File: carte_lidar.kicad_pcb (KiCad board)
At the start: 2 copper layers, 68 x 68 mm, 26 parts, among them J1 Conn_01x03_Pin, J2 Conn_01x02_Pin, J3 Conn_01x05_Socket, J4 Conn_01x02, J5 Conn_01x08_Pin, U1 TPS54302, U2 RP2040, U3 CH340C

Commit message: v1
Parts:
- removed U3: CH340C, Package_SO:SOIC-16_3.9x9.9mm_P1.27mm
- added R5: 330R, Resistor_SMD:R_0603_1608Metric, F.Cu at (84.5, 102.5)
- J5: value Conn_01x08_Pin -> Conn_01x04_Socket; footprint Connector_PinHeader_1.00mm:PinHeader_1x08_P1.00mm_Vertical -> Connector_PinSocket_2.54mm:PinSocket_1x04_P2.54mm_Vertical
- U2: value RP2040 -> Pico; footprint Package_DFN_QFN:QFN-56-1EP_7x7mm_P0.4mm_EP3.2x3.2mm -> MCU_RaspberryPi_and_Boards:RPi_Pico_SMD_TH
- moved J3 50.8 mm to (86.3, 76.0), turned to -90 degrees
- moved C6 43.0 mm to (91.5, 126.5), turned to -90 degrees
- moved J4 42.1 mm to (125.9, 104.0), turned to 90 degrees
- moved C8 42.1 mm to (93.7, 126.4), turned to -90 degrees
- moved C7 41.2 mm to (89.3, 126.5), turned to -90 degrees
- moved J5 40.4 mm to (84.8, 91.9)
- moved J1 40.1 mm to (75.8, 94.3), turned to -90 degrees
- moved C9 34.2 mm to (91.7, 119.6)
- moved R4 33.7 mm to (125.3, 109.2)
- moved R3 33.0 mm to (125.3, 110.4)
- moved C10 32.7 mm to (89.5, 119.6)
- moved L1 30.9 mm to (84.0, 123.5), turned to 0 degrees
- moved C3 25.5 mm to (86.1, 118.9)
- moved J2 24.9 mm to (81.0, 107.0), turned to -90 degrees
- moved R1 21.4 mm to (76.3, 119.4), turned to 90 degrees
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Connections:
- J1 pad 1: unconnected-(J1-Pin_1-Pad1) -> 5V
- J1 pad 2: unconnected-(J1-Pin_2-Pad2) -> GND
- J1 pad 3: unconnected-(J1-Pin_3-Pad3) -> /led
- J3 pad 1: unconnected-(J3-Pin_1-Pad1) -> 5V
- J3 pad 2: unconnected-(J3-Pin_2-Pad2) -> /lidar_tx
- J3 pad 3: unconnected-(J3-Pin_3-Pad3) -> /lidar_rx
- J3 pad 4: unconnected-(J3-Pin_4-Pad4) -> GND
- J3 pad 5: unconnected-(J3-Pin_5-Pad5) -> /motoct
- J5 pad 1: unconnected-(J5-Pin_1-Pad1) -> 5V
- J5 pad 2: unconnected-(J5-Pin_2-Pad2) -> GND
- J5 pad 3: unconnected-(J5-Pin_3-Pad3) -> /scl
- J5 pad 4: unconnected-(J5-Pin_4-Pad4) -> /sda
- U2 pad 1: Net-(U2-IOVDD-Pad1) -> AU
- U2 pad 10: Net-(U2-IOVDD-Pad1) -> unconnected-(U2-GPIO7-Pad10)
- U2 pad 11: unconnected-(U2-GPIO8-Pad11) -> /sda
- U2 pad 12: unconnected-(U2-GPIO9-Pad12) -> /scl
- U2 pad 13: unconnected-(U2-GPIO10-Pad13) -> GND
- U2 pad 15: unconnected-(U2-GPIO12-Pad15) -> /motoct
- U2 pad 16: unconnected-(U2-GPIO13-Pad16) -> /lidar_rx
- U2 pad 17: unconnected-(U2-GPIO14-Pad17) -> /lidar_tx
- U2 pad 18: unconnected-(U2-GPIO15-Pad18) -> GND
- U2 pad 22: Net-(U2-IOVDD-Pad1) -> unconnected-(U2-GPIO17-Pad22)
- U2 pad 23: Net-(U2-DVDD-Pad23) -> GND
- U2 pad 28: unconnected-(U2-GPIO17-Pad28) -> GND
- U2 pad 3: unconnected-(U2-GPIO1-Pad3) -> GND
- U2 pad 33: Net-(U2-IOVDD-Pad1) -> unconnected-(U2-AGND-Pad33)
- U2 pad 38: unconnected-(U2-GPIO26_ADC0-Pad38) -> GND
- U2 pad 39: unconnected-(U2-GPIO27_ADC1-Pad39) -> 5V
- U2 pad 40: unconnected-(U2-GPIO28_ADC2-Pad40) -> 5V
- U2 pad 42: Net-(U2-IOVDD-Pad1) -> GND
- U2 pad 6: unconnected-(U2-GPIO4-Pad6) -> Net-(U2-GPIO4)
- U2 pad 8: unconnected-(U2-GPIO6-Pad8) -> GND
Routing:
- net 5V: track 0.00 -> 133.8 mm
- net GND: track 0.00 -> 40.0 mm, vias 0 -> 1
- net Net-(U2-GPIO4): track 0.00 -> 34.2 mm
- net /scl: track 0.00 -> 31.9 mm
- net /sda: track 0.00 -> 31.7 mm
- net /lidar_rx: track 0.00 -> 31.6 mm
- net /lidar_tx: track 0.00 -> 31.6 mm
- net /motoct: track 0.00 -> 30.6 mm
- net AU: track 0.00 -> 19.3 mm
- net /led: track 0.00 -> 10.3 mm
- net Net-(U1-FB): track 0.00 -> 9.81 mm
- net Net-(U1-SW): track 0.00 -> 9.74 mm
- net Net-(J4-Pin_1): track 0.00 -> 5.05 mm
- net Net-(U1-BOOT): track 0.00 -> 2.37 mm
- net 24V: track 0.00 -> 1.72 mm
- added copper zone on F.Cu, net 24V
- added copper zone on F.Cu, net 5V
- added copper zone on B.Cu, net GND
- added copper zone on F.Cu, net GND
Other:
- board text added: "Accelerometer"
- board text added: "LED"
- board text added: "LIDAR"
- board text added: "VIN - 24V"

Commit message: update all
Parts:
- added C21: 0.1uF 10V, Capacitor_SMD:C_0402_1005Metric, F.Cu at (101.8, 103.6)
- added C22: 220nF 50V, Capacitor_SMD:C_0402_1005Metric, F.Cu at (69.7, 107.7)
- added C23: 2.2nF 10V, Capacitor_SMD:C_0402_1005Metric, F.Cu at (103.4, 98.3)
- added C24: 0.1uF 10V, Capacitor_SMD:C_0402_1005Metric, F.Cu at (103.4, 101.8)
- added C25: 0.1uF 10V, Capacitor_SMD:C_0402_1005Metric, F.Cu at (108.9, 88.0)
- added C26: 1uF 10V, Capacitor_SMD:C_0402_1005Metric, F.Cu at (108.6, 90.8)
- added C27: 0.1uF 10V, Capacitor_SMD:C_0402_1005Metric, F.Cu at (96.8, 89.0)
- added C28: 220nF 16V, Capacitor_SMD:C_0402_1005Metric, F.Cu at (119.0, 79.4)
- added D1: MBR120VLSFT1G, Diode_SMD:D_SOD-123F, F.Cu at (123.2, 101.4)
- added J6: USB_C_Receptacle_USB2.0, Connector_USB:USB_C_Receptacle_GCT_USB4105-xx-A_16P_TopMnt_Horizontal, F.Cu at (125.7, 94.5)
- added LED1: YELLOW, LED_SMD:LED_0805_2012Metric, F.Cu at (124.8, 104.8)
- added LED2: YELLOW, LED_SMD:LED_0805_2012Metric, F.Cu at (87.9, 91.2)
- added R11: 5.1k, Resistor_SMD:R_0402_1005Metric, F.Cu at (119.0, 94.0)
- added R12: 5.1k, Resistor_SMD:R_0402_1005Metric, F.Cu at (119.0, 92.8)
- added R13: 27R, Resistor_SMD:R_0402_1005Metric, F.Cu at (115.7, 96.8)
- added R14: 27R, Resistor_SMD:R_0402_1005Metric, F.Cu at (115.7, 95.7)
- added R15: 1k, Resistor_SMD:R_0402_1005Metric, F.Cu at (88.9, 93.4)
- added R16: 10k, Capacitor_SMD:C_0402_1005Metric, F.Cu at (96.9, 91.0)
- added R17: 5.1k, Resistor_SMD:R_0402_1005Metric, F.Cu at (68.3, 105.9)
- added R18: 1k, Resistor_SMD:R_0402_1005Metric, F.Cu at (70.0, 106.4)
- added R6: 1k, Resistor_SMD:R_0402_1005Metric, F.Cu at (104.6, 73.3)
- added R7: 100k, Resistor_SMD:R_0402_1005Metric, F.Cu at (104.6, 74.7)
- added R8: 1k, Resistor_SMD:R_0402_1005Metric, F.Cu at (122.1, 103.8)
- added SW1: SW_Push, Button_Switch_SMD:SW_SPST_B3U-1000P, F.Cu at (104.1, 69.9)
- added U3: W25Q128JVS, Package_SO:SOIC-8_5.23x5.23mm_P1.27mm, F.Cu at (113.6, 80.8)
- added U5: USBLC6-2P6, Package_TO_SOT_SMD:SOT-666, F.Cu at (119.1, 96.2)
- added U6: NM/AMS1117-3.3, Package_TO_SOT_SMD:SOT-223-3_TabPin2, F.Cu at (116.1, 103.8)
- added U7: MPU-6000, Sensor_Motion:InvenSense_QFN-24_4x4mm_P0.5mm, F.Cu at (100.0, 100.0)
- added X1: S2D12.000000B20F30T, Oscillator:Oscillator_SMD_ECS_2520MV-xxx-xx-4Pin_2.5x2.0mm, F.Cu at (93.6, 90.0)
- J1, J2, J3, J4: moved to B.Cu
- J5: value Conn_01x04_Socket -> Conn_01x02_Pin; footprint Connector_PinSocket_2.54mm:PinSocket_1x04_P2.54mm_Vertical -> Connector_PinHeader_2.54mm:PinHeader_1x02_P2.54mm_Vertical
- U2: value Pico -> RP2040; footprint MCU_RaspberryPi_and_Boards:RPi_Pico_SMD_TH -> Package_DFN_QFN:QFN-56-1EP_7x7mm_P0.4mm_EP3.2x3.2mm_ThermalVias
- moved H2 59.0 mm to (74.5, 85.2)
- moved C6 35.7 mm to (77.6, 93.6), turned to 90 degrees
- moved C8 34.8 mm to (81.8, 93.7), turned to 90 degrees
- moved C7 34.2 mm to (79.7, 93.7), turned to 90 degrees
- moved H3 29.6 mm to (100.0, 129.5)
- moved C10 29.5 mm to (75.5, 93.6)
- moved H1 29.5 mm to (125.5, 85.2)
- moved J4 27.9 mm to (109.0, 126.3), turned to 180 degrees
- moved C9 27.1 mm to (83.9, 93.7)
- moved J5 25.2 mm to (99.0, 71.1), turned to 180 degrees
- moved L1 24.6 mm to (78.1, 99.7), turned to 90 degrees
- moved J3 22.7 mm to (89.5, 98.5)
- moved C5 21.8 mm to (84.8, 99.4), turned to -90 degrees
- moved R1 21.8 mm to (82.6, 98.5), turned to -90 degrees
- moved R5 21.3 mm to (88.4, 81.6)
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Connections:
- net 24V renamed /power/VBAT
- C10 pad 1: 5V -> +5V
- C5 pad 1: 5V -> +5V
- C6 pad 1: 5V -> +5V
- C7 pad 1: 5V -> +5V
- C8 pad 1: 5V -> +5V
- C9 pad 1: 5V -> +5V
- J1 pad 1: 5V -> +5V
- J1 pad 3: /led -> Net-(J1-Pin_3)
- J3 pad 1: 5V -> +5V
- J5 pad 1: 5V -> Net-(J5-Pin_1)
- L1 pad 2: 5V -> +5V
- R1 pad 1: 5V -> +5V
- R3 pad 1: AU -> /AU
- R4 pad 1: 5V -> +3V3
- R5 pad 1: /led -> Net-(J1-Pin_3)
- R5 pad 2: Net-(U2-GPIO4) -> /led
- U2 pad 1: AU -> +3V3
- U2 pad 10: unconnected-(U2-GPIO7-Pad10) -> +3V3
- U2 pad 11: /sda -> unconnected-(U2-GPIO8-Pad11)
- U2 pad 12: /scl -> unconnected-(U2-GPIO9-Pad12)
- U2 pad 13: GND -> unconnected-(U2-GPIO10-Pad13)
- U2 pad 15: /motoct -> /led
- U2 pad 16: /lidar_rx -> unconnected-(U2-GPIO13-Pad16)
- U2 pad 17: /lidar_tx -> unconnected-(U2-GPIO14-Pad17)
- U2 pad 18: GND -> unconnected-(U2-GPIO15-Pad18)
- U2 pad 19: unconnected-(U2-GPIO14-Pad19) -> GND
- U2 pad 22: unconnected-(U2-GPIO17-Pad22) -> +3V3
- U2 pad 23: GND -> /+1.1V
- U2 pad 24: unconnected-(U2-GPIO18-Pad24) -> /Clk_12MHz
- U2 pad 26: unconnected-(U2-GPIO20-Pad26) -> Net-(U2-RUN)
- U2 pad 28: GND -> unconnected-(U2-GPIO17-Pad28)
- U2 pad 3: GND -> unconnected-(U2-GPIO1-Pad3)
- U2 pad 30: unconnected-(U2-RUN-Pad30) -> /motoct
- U2 pad 31: unconnected-(U2-GPIO26_ADC0-Pad31) -> /lidar_tx
- U2 pad 32: unconnected-(U2-GPIO27_ADC1-Pad32) -> /lidar_rx
- U2 pad 33: unconnected-(U2-AGND-Pad33) -> +3V3
- U2 pad 37: unconnected-(U2-3V3_EN-Pad37) -> /AU
- U2 pad 38: GND -> BAT_SENSE
- U2 pad 39: 5V -> unconnected-(U2-GPIO27_ADC1-Pad39)
- U2 pad 40: 5V -> unconnected-(U2-GPIO28_ADC2-Pad40)
- U2 pad 42: GND -> +3V3
- U2 pad 43: unconnected-(U2-SWDIO-Pad43) -> +3V3
- U2 pad 6: Net-(U2-GPIO4) -> /MISO
- U2 pad 7: unconnected-(U2-GPIO5-Pad7) -> /CSn
- U2 pad 8: GND -> /SCLK
- U2 pad 9: unconnected-(U2-GPIO6-Pad9) -> /MOSI
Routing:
- net 5V: track 133.8 -> 0.00 mm
- net BAT_SENSE: track 0.00 -> 71.4 mm
- net +5V: track 0.00 -> 34.3 mm
- net Net-(U2-GPIO4): track 34.2 -> 0.00 mm
- net /AU: track 0.00 -> 33.1 mm, vias 0 -> 2
- net /CSn: track 0.00 -> 32.4 mm, vias 0 -> 2
- net /scl: track 31.9 -> 0.00 mm
- net /sda: track 31.7 -> 0.00 mm
- net /MISO: track 0.00 -> 26.6 mm, vias 0 -> 2
- net Net-(D1-A): track 0.00 -> 26.3 mm
- net /power/VBAT: track 1.72 -> 27.3 mm
- net AU: track 19.3 -> 0.00 mm
- net Net-(U2-QSPI_SD3): track 0.00 -> 18.4 mm
- net /MOSI: track 0.00 -> 18.3 mm, vias 0 -> 2
- net Net-(U2-QSPI_SS): track 0.00 -> 17.9 mm
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- added copper zone on F.Cu, net +3V3
- added copper zone on In2.Cu, net +3V3
- added copper zone on F.Cu, net +5V
- added copper zone on In1.Cu, net GND
- removed copper zone on F.Cu, net 5V
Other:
- copper layers 2 -> 4
- board text added: "Opossum carte lidar 2025"
- board text removed: "Accelerometer"
- board text removed: "LED"
- board text removed: "LIDAR"
- board text removed: "VIN - 24V"

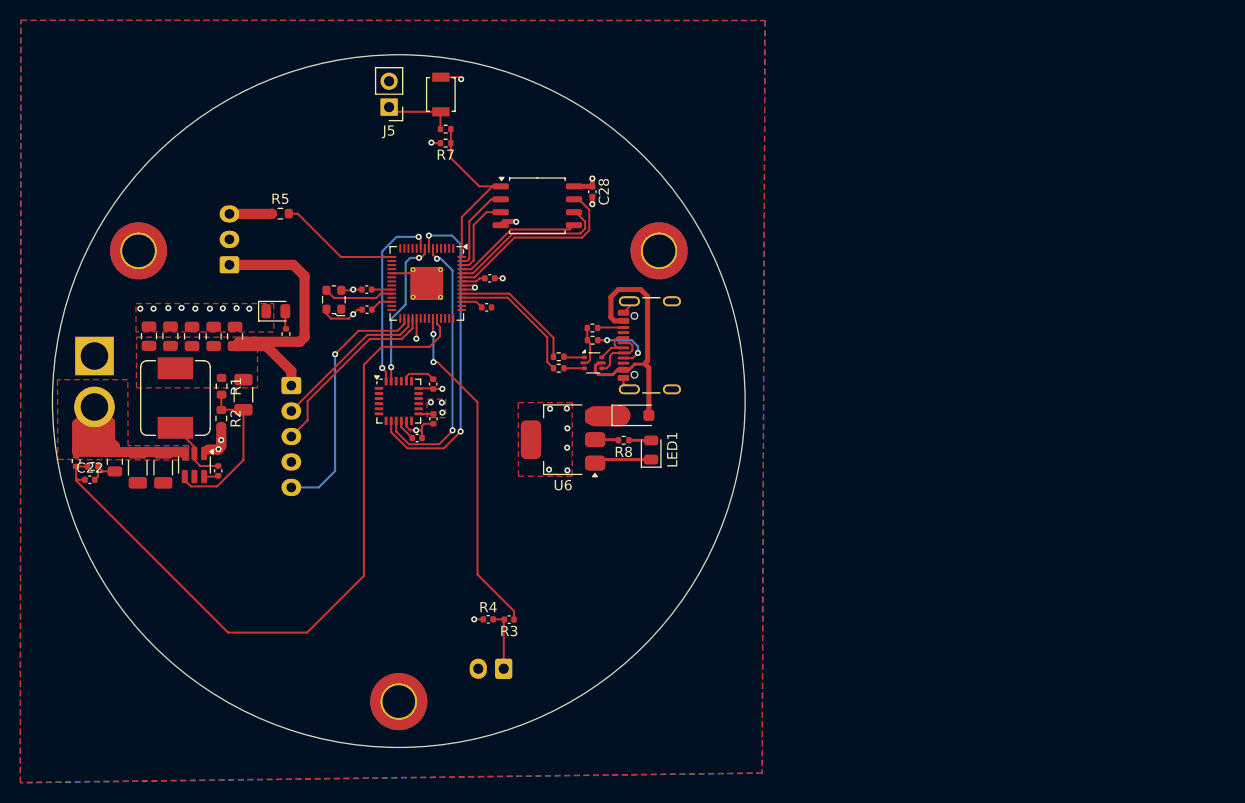
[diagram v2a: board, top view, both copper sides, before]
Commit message: add ethernet in schematic
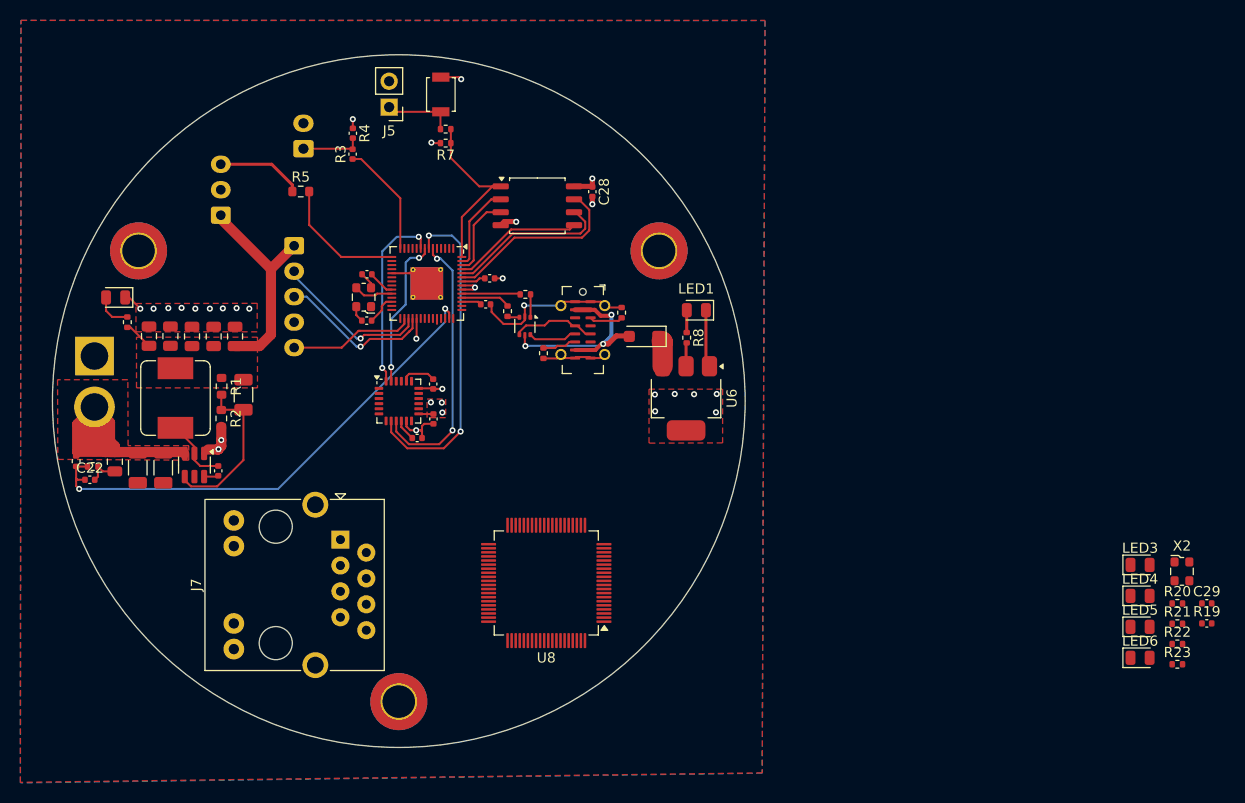
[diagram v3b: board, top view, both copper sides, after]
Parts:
- removed J6: USB_C_Receptacle_USB2.0, Connector_USB:USB_C_Receptacle_GCT_USB4105-xx-A_16P_TopMnt_Horizontal
- added C29: 10nF, Capacitor_SMD:C_0402_1005Metric, F.Cu at (179.3, 119.9)
- added J7: RJ45_LED_Shielded, Connector_RJ:RJ45_BEL_SS74301-00x_Vertical, F.Cu at (94.3, 113.6)
- added J8: USB_C_Receptacle_USB2.0_16P, Connector_USB:USB_C_Receptacle_G-Switch_GT-USB-7051x, F.Cu at (118.1, 93.0)
- added LED3: green, LED_SMD:LED_0805_2012Metric, F.Cu at (172.8, 116.1)
- added LED4: green, LED_SMD:LED_0805_2012Metric, F.Cu at (172.8, 119.1)
- added LED5: green, LED_SMD:LED_0805_2012Metric, F.Cu at (172.8, 122.2)
- added LED6: green, LED_SMD:LED_0805_2012Metric, F.Cu at (172.8, 125.2)
- added R19: 12.4k 1%, Capacitor_SMD:C_0402_1005Metric, F.Cu at (179.3, 121.8)
- added R20: 1k, Resistor_SMD:R_0402_1005Metric, F.Cu at (176.4, 119.9)
- added R21: 1k, Resistor_SMD:R_0402_1005Metric, F.Cu at (176.4, 121.9)
- added R22: 1k, Resistor_SMD:R_0402_1005Metric, F.Cu at (176.4, 123.8)
- added R23: 1k, Resistor_SMD:R_0402_1005Metric, F.Cu at (176.4, 125.8)
- added U8: W5500, Package_QFP:LQFP-80_10x10mm_P0.4mm, F.Cu at (114.5, 117.8)
- added X2: S2D25.000000B20F30T, Oscillator:Oscillator_SMD_ECS_2520MV-xxx-xx-4Pin_2.5x2.0mm, F.Cu at (176.9, 116.7)
- moved J4 55.4 mm to (90.6, 74.0), turned to 90 degrees
- moved R4 49.5 mm to (95.5, 73.7), turned to -90 degrees
- moved R3 48.2 mm to (95.5, 75.8), turned to 90 degrees
- moved LED2 15.8 mm to (72.2, 89.8), turned to 180 degrees
- moved R15 15.6 mm to (73.3, 92.2)
- moved LED1 14.4 mm to (129.2, 91.1), turned to 180 degrees
- moved J3 13.7 mm to (89.7, 84.8)
- moved U6 12.7 mm to (128.2, 99.7), turned to -90 degrees
- moved R8 11.8 mm to (128.3, 93.8), turned to -90 degrees
- moved D1 7.80 mm to (124.0, 93.7), turned to 180 degrees
- moved U5 7.62 mm to (112.4, 92.6), turned to -90 degrees
- moved R13 7.52 mm to (110.7, 91.2), turned to 90 degrees
- moved R14 6.95 mm to (112.4, 89.5)
- moved R12 5.41 mm to (114.2, 95.3), turned to -90 degrees
- moved J1 4.95 mm to (82.5, 79.2)
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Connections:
- U2 pad 14: unconnected-(U2-GPIO11-Pad14) -> /AU
- U2 pad 17: unconnected-(U2-GPIO14-Pad17) -> eth_pmode2
- U2 pad 18: unconnected-(U2-GPIO15-Pad18) -> eth_pmode1
- U2 pad 27: unconnected-(U2-GPIO16-Pad27) -> eth_pmode0
- U2 pad 34: unconnected-(U2-GPIO22-Pad34) -> eth_rst
- U2 pad 35: unconnected-(U2-GPIO23-Pad35) -> eth_int
- U2 pad 36: unconnected-(U2-GPIO24-Pad36) -> eth_miso
- U2 pad 37: /AU -> eth_scs
- U2 pad 38: BAT_SENSE -> eth_sclk
- U2 pad 39: unconnected-(U2-GPIO27_ADC1-Pad39) -> eth_mosi
- U2 pad 41: unconnected-(U2-GPIO29_ADC3-Pad41) -> BAT_SENSE
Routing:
- net BAT_SENSE: track 71.4 -> 49.5 mm, vias 0 -> 2
- net /AU: track 33.1 -> 11.2 mm, vias 2 -> 0
- net GND: track 37.8 -> 55.0 mm
- net /motoct: track 25.0 -> 12.3 mm, vias 1 -> 0
- net +5V: track 34.3 -> 24.3 mm
- net USB_N: track 13.3 -> 4.86 mm
- net USB_P: track 12.7 -> 5.76 mm
- net Net-(J1-Pin_3): track 4.19 -> 8.69 mm
- net Net-(D1-A): track 26.3 -> 22.4 mm, vias 0 -> 3
- net Net-(J8-CC1): track 6.46 -> 3.30 mm, vias 2 -> 0
- net /Clk_12MHz: track 6.90 -> 3.87 mm
- net /lidar_rx: track 18.4 -> 15.4 mm, vias 0 -> 1
- net +3V3: track 17.5 -> 14.6 mm, vias 15 -> 14
- net Net-(J8-D--PadA7): track 5.71 -> 8.51 mm
- net Net-(LED2-A): track 1.77 -> 3.65 mm
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
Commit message: update all
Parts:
- removed C29: 10nF, Capacitor_SMD:C_0402_1005Metric
- removed J7: RJ45_LED_Shielded, Connector_RJ:RJ45_BEL_SS74301-00x_Vertical
- removed LED3, LED4, LED5, LED6: green, LED_SMD:LED_0805_2012Metric
- removed R19: 12.4k 1%, Capacitor_SMD:C_0402_1005Metric
- removed R20, R21, R22, R23: 1k, Resistor_SMD:R_0402_1005Metric
- removed U8: W5500, Package_QFP:LQFP-80_10x10mm_P0.4mm
- removed X2: S2D25.000000B20F30T, Oscillator:Oscillator_SMD_ECS_2520MV-xxx-xx-4Pin_2.5x2.0mm
- added J10: Conn_01x06_Socket, Connector_JST:JST_XH_B6B-XH-AM_1x06_P2.50mm_Vertical, F.Cu at (88.9, 115.2)
- added J11: Conn_01x06_Socket, Connector_JST:JST_XH_B6B-XH-AM_1x06_P2.50mm_Vertical, F.Cu at (89.0, 122.5)
- added J12: Conn_01x06_Socket, Connector_JST:JST_XH_B6B-XH-AM_1x06_P2.50mm_Vertical, F.Cu at (88.8, 108.1)
- added J6: Conn_01x06_Socket, Connector_PinHeader_2.54mm:PinHeader_1x06_P2.54mm_Vertical, F.Cu at (109.0, 120.9)
- added J9: Conn_01x06_Socket, Connector_PinHeader_2.54mm:PinHeader_1x06_P2.54mm_Vertical, F.Cu at (121.7, 100.6)
- added R24: 4.7k, Resistor_SMD:R_0402_1005Metric, F.Cu at (92.7, 128.4)
- added R25: 4.7k, Resistor_SMD:R_0402_1005Metric, F.Cu at (92.7, 127.3)
- moved J3 10.4 mm to (90.4, 95.1), turned to 90 degrees
- moved R11 0.83 mm to (122.7, 91.3)
- moved C27 0.35 mm to (96.5, 87.5)
- moved X1 0.22 mm to (96.3, 89.8)
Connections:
- U2 pad 16: unconnected-(U2-GPIO13-Pad16) -> tof3
- U2 pad 17: eth_pmode2 -> unconnected-(U2-GPIO14-Pad17)
- U2 pad 18: eth_pmode1 -> unconnected-(U2-GPIO15-Pad18)
- U2 pad 2: unconnected-(U2-GPIO0-Pad2) -> sda
- U2 pad 27: eth_pmode0 -> unconnected-(U2-GPIO16-Pad27)
- U2 pad 3: unconnected-(U2-GPIO1-Pad3) -> scl
- U2 pad 4: unconnected-(U2-GPIO2-Pad4) -> tof2
- U2 pad 5: unconnected-(U2-GPIO3-Pad5) -> tof1
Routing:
- net tof2: track 0.00 -> 95.0 mm, vias 0 -> 1
- net tof1: track 0.00 -> 81.0 mm, vias 0 -> 1
- net sda: track 0.00 -> 67.1 mm, vias 0 -> 2
- net scl: track 0.00 -> 59.1 mm, vias 0 -> 2
- net eth_mosi: track 0.00 -> 54.1 mm
- net eth_scs: track 0.00 -> 47.6 mm
- net eth_int: track 0.00 -> 43.5 mm
- net eth_sclk: track 0.53 -> 35.0 mm, vias 0 -> 1
- net tof3: track 0.00 -> 33.7 mm, vias 0 -> 1
- net +3V3: track 14.6 -> 46.0 mm, vias 14 -> 22
- net eth_miso: track 0.00 -> 23.7 mm, vias 0 -> 1
- net eth_rst: track 0.00 -> 23.2 mm, vias 0 -> 1
- net /MISO: track 26.6 -> 44.0 mm
- net /CSn: track 32.4 -> 41.6 mm
- net Net-(J8-D--PadA7): track 8.51 -> 16.7 mm, vias 0 -> 2
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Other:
- board text added: "3V3"
- board text added: "3v3"
- board text added: "5V"
- board text added: "AU"
- board text added: "Ethernet W5500"
- board text added: "GND"
- board text added: "LED"
- board text added: "RX"
- board text added: "SW1"
- board text added: "TOF1"
- board text added: "TOF2"
- board text added: "TOF3"
- board text added: "TX"
- board text added: "Vin - 24V"
- board text added: "gnd"
- board text added: "int"
- board text added: "miso"
- board text added: "mosi"
- board text added: "motor"
- board text added: "power by usb"
- board text added: "rst"
- board text added: "scl"
- board text added: "sclk"
- board text added: "scs"
- board text added: "sda"
